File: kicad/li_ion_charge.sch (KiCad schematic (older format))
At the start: 17 parts, among them P101 USB_B, P102 CONN_01X02, P103 CONN_01X02, U101 MCP73834-FCI/UN

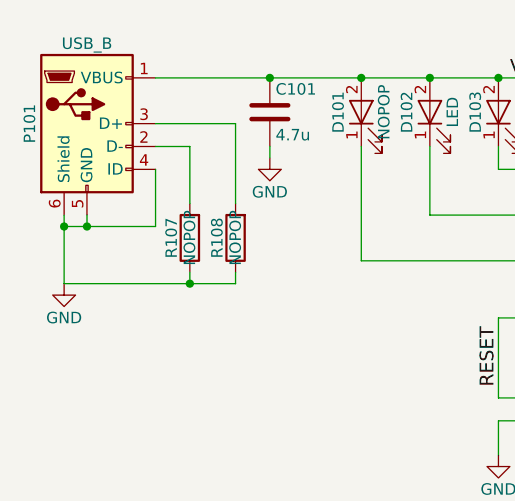
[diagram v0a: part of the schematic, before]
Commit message: Update schematic and netlist to include a new nopop resistor, and this should be close to what the final part placement on the layout should look like
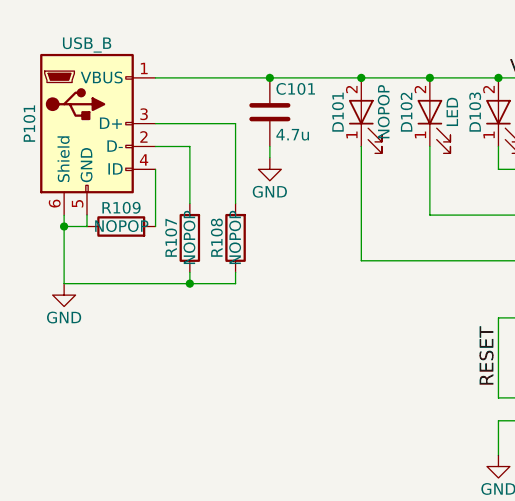
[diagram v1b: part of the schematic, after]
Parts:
- added R109: NOPOP, Resistors_SMD:R_0805_HandSoldering, symbol R
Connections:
- net GND: now also R109.1; no longer P101.4 (ID)
- new net: P101.4 (ID), R109.2
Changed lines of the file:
@@
 	3150 4000 3150 3750
 Wire Wire Line
-	2750 4000 3150 4000
-Wire Wire Line
 	2750 3950 2750 4250
-Connection ~ 2750 4000
 Wire Wire Line
 	2850 3950 2850 4000
-Connection ~ 2850 4000
 $Comp
 L GND #PWR04
@@
 	3300 4200 3300 4250
 Connection ~ 3300 4250
+$Comp
+L R R109
+U 1 1 58C58F65
+P 3000 4000
+F 0 "R109" V 3080 4000 50  0000 C CNN
+F 1 "NOPOP" V 3000 4000 50  0000 C CNN
+F 2 "Resistors_SMD:R_0805_HandSoldering" V 2930 4000 50  0001 C CNN
+F 3 "" H 3000 4000 50  0000 C CNN
+	1    3000 4000
+	0    -1   -1   0
+$EndComp
+Wire Wire Line
+	2850 4000 2750 4000
+Connection ~ 2750 4000
 $EndSCHEMATC

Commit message: initial BOM
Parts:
- added J?: CONN_01X02, symbol CONN_01X02
- C101, C102: MPN (none) -> LMK316B7475KL-T
- D102, D103: MPN (none) -> LTST-S220GKT
- P102: MPN (none) -> M20-9990246
- P103: footprint Pin_Headers:Pin_Header_Straight_1x02_Pitch2.54mm -> Pin_Headers:Pin_Header_Straight_1x02_Pitch2.00mm; MPN (none) -> M20-9990246
- R101, R102: MPN (none) -> RMCF0805JT470R
- R104: MPN (none) -> RC0805JR-071KL
- R105: MPN (none) -> RC0805JR-0710KL
- R106: MPN (none) -> ERJ-6ENF2001V
- U101: value MCP73834-FCI/UN -> MCP73834; MPN (none) -> MCP73834-FCI/UN
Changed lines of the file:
@@
 F 1 "LED" H 4650 3400 50  0000 C CNN
 F 2 "LEDs:LED_0805" H 4650 3500 50  0001 C CNN
-F 3 "" H 4650 3500 50  0000 C CNN
+F 3 "https://media.digikey.com/pdf/Data%20Sheets/Lite-On%20PDFs/LTST-S220GKT.pdf" H 4650 3500 50  0001 C CNN
+F 4 "LTST-S220GKT" H 4650 3500 60  0001 C CNN "MPN"
 	1    4650 3500
 	0    -1   -1   0
@@
 F 1 "LED" H 4350 3400 50  0000 C CNN
 F 2 "LEDs:LED_0805" H 4350 3500 50  0001 C CNN
-F 3 "" H 4350 3500 50  0000 C CNN
+F 3 "https://media.digikey.com/pdf/Data%20Sheets/Lite-On%20PDFs/LTST-S220GKT.pdf" H 4350 3500 50  0001 C CNN
+F 4 "LTST-S220GKT" H 4350 3500 60  0001 C CNN "MPN"
 	1    4350 3500
 	0    -1   -1   0
@@
 F 2 "Resistors_SMD:R_0805_HandSoldering" V 4930 3950 50  0001 C CNN
 F 3 "" H 5000 3950 50  0000 C CNN
+F 4 "RMCF0805JT470R" V 5000 3950 60  0001 C CNN "MPN"
 	1    5000 3950
 	0    1    1    0
@@
 F 2 "Resistors_SMD:R_0805_HandSoldering" V 4930 3750 50  0001 C CNN
 F 3 "" H 5000 3750 50  0000 C CNN
+F 4 "RMCF0805JT470R" V 5000 3750 60  0001 C CNN "MPN"
 	1    5000 3750
 	0    1    1    0
@@
 P 5800 3700
 F 0 "U101" H 6050 3150 60  0000 C CNN
-F 1 "MCP73834-FCI/UN" H 5850 4250 60  0000 C CNN
+F 1 "MCP73834" H 5850 4250 60  0000 C CNN
 F 2 "Housings_SSOP:MSOP-10_3x3mm_Pitch0.5mm" H 5800 3700 60  0001 C CNN
-F 3 "" H 5800 3700 60  0001 C CNN
+F 3 "http://ww1.microchip.com/downloads/en/DeviceDoc/22005a.pdf" H 5800 3700 60  0001 C CNN
+F 4 "MCP73834-FCI/UN" H 5800 3700 60  0001 C CNN "MPN"
 	1    5800 3700
 	1    0    0    -1
@@
 F 2 "Resistors_SMD:R_0805_HandSoldering" V 6580 3950 50  0001 C CNN
 F 3 "" H 6650 3950 50  0000 C CNN
+F 4 "ERJ-6ENF2001V" V 6650 3950 60  0001 C CNN "MPN"
 	1    6650 3950
 	0    1    1    0
@@
 F 2 "Resistors_SMD:R_0805_HandSoldering" V 6580 3750 50  0001 C CNN
 F 3 "" H 6650 3750 50  0000 C CNN
+F 4 "RC0805JR-0710KL" V 6650 3750 60  0001 C CNN "MPN"
 	1    6650 3750
 	0    1    1    0
@@
 F 1 "4.7u" H 7275 3650 50  0000 L CNN
 F 2 "Capacitors_SMD:C_1206_HandSoldering" H 7288 3600 50  0001 C CNN
-F 3 "" H 7250 3750 50  0000 C CNN
+F 3 "http://www.yuden.co.jp/productdata/catalog/en/mlcc_all_e.pdf" H 7250 3750 50  0001 C CNN
+F 4 "LMK316B7475KL-T" H 7250 3750 60  0001 C CNN "MPN"
 	1    7250 3750
 	1    0    0    -1
@@
 F 0 "P103" H 7700 3550 50  0000 C CNN
 F 1 "CONN_01X02" V 7800 3400 50  0000 C CNN
-F 2 "Pin_Headers:Pin_Header_Straight_1x02_Pitch2.54mm" H 7700 3400 50  0001 C CNN
+F 2 "Pin_Headers:Pin_Header_Straight_1x02_Pitch2.00mm" H 7700 3400 50  0001 C CNN
 F 3 "" H 7700 3400 50  0000 C CNN
+F 4 "M20-9990246" H 7700 3400 60  0001 C CNN "MPN"
 	1    7700 3400
 	1    0    0    -1
@@
 F 1 "4.7u" H 3675 3400 50  0000 L CNN
 F 2 "Capacitors_SMD:C_1206_HandSoldering" H 3688 3350 50  0001 C CNN
-F 3 "" H 3650 3500 50  0000 C CNN
+F 3 "http://www.yuden.co.jp/productdata/catalog/en/mlcc_all_e.pdf" H 3650 3500 50  0001 C CNN
+F 4 "LMK316B7475KL-T" H 3650 3500 60  0001 C CNN "MPN"
 	1    3650 3500
 	1    0    0    -1
@@
 F 2 "Resistors_SMD:R_0805_HandSoldering" V 4930 4400 50  0001 C CNN
 F 3 "" H 5000 4400 50  0000 C CNN
+F 4 "RC0805JR-071KL" V 5000 4400 60  0001 C CNN "MPN"
 	1    5000 4400
 	0    1    1    0
@@
 F 2 "Pin_Headers:Pin_Header_Straight_1x02_Pitch2.54mm" H 4950 4800 50  0001 C CNN
 F 3 "" H 4950 4800 50  0000 C CNN
+F 4 "M20-9990246" H 4950 4800 60  0001 C CNN "MPN"
 	1    4950 4800
 	1    0    0    -1
@@
 	2850 4000 2750 4000
 Connection ~ 2750 4000
+$Comp
+L CONN_01X02 J?
+U 1 1 58D86672
+P 7950 4900
+F 0 "J?" H 7950 5050 50  0000 C CNN
+F 1 "CONN_01X02" V 8050 4900 50  0000 C CNN
+F 2 "" H 7950 4900 50  0001 C CNN
+F 3 "http://www.jst-mfg.com/product/pdf/eng/ePH.pdf" H 7950 4900 50  0001 C CNN
+F 4 "B2B-PH-K-S(LF)(SN)" H 7950 4900 60  0001 C CNN "MPN"
+	1    7950 4900
+	1    0    0    -1
+$EndComp
 $EndSCHEMATC

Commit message: Minor schematic change
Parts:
- gave numbers to parts that had none: 1
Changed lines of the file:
@@
 Connection ~ 2750 4000
 $Comp
-L CONN_01X02 J?
+L CONN_01X02 J101
 U 1 1 58D86672
 P 7950 4900
-F 0 "J?" H 7950 5050 50  0000 C CNN
+F 0 "J101" H 7950 5050 50  0000 C CNN
 F 1 "CONN_01X02" V 8050 4900 50  0000 C CNN
 F 2 "" H 7950 4900 50  0001 C CNN
